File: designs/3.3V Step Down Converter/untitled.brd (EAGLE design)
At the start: 25 x 30 mm, 10 parts, among them IC1 TPS62160DGKR, J1 S2B-PH-SM4, J2 S2B-PH-SM4

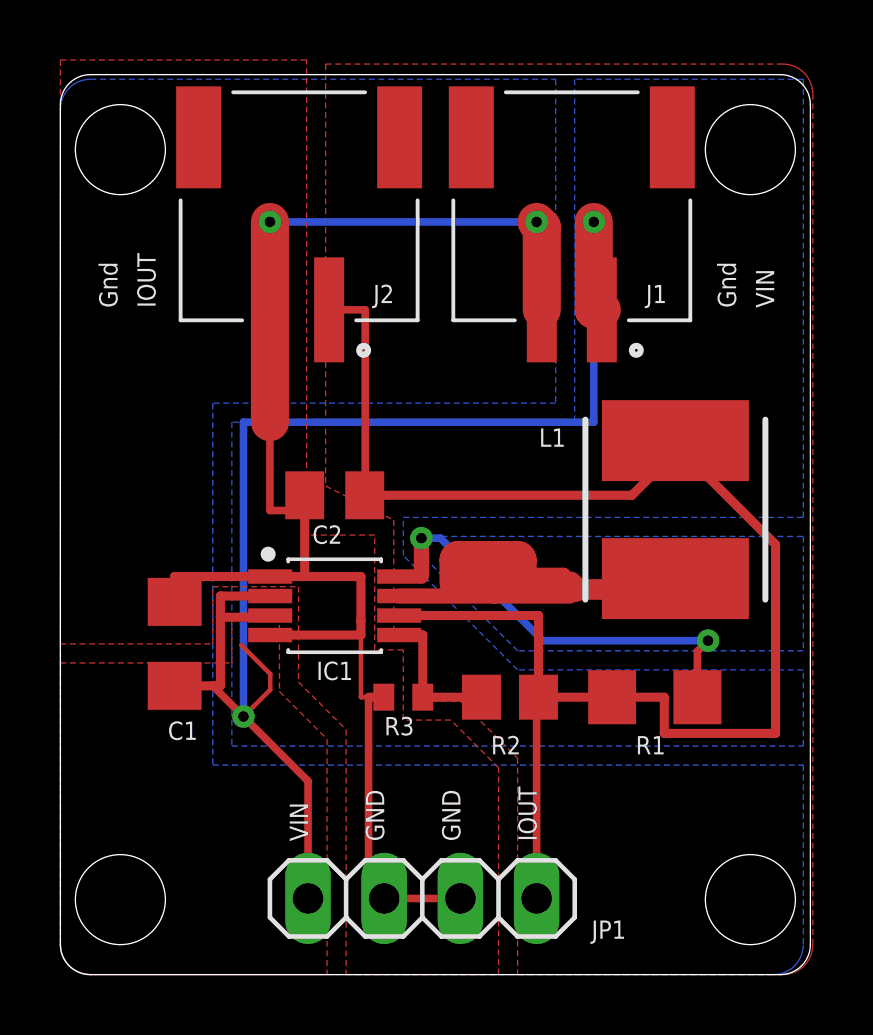
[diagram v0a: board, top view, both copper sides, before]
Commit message: added design block Logo
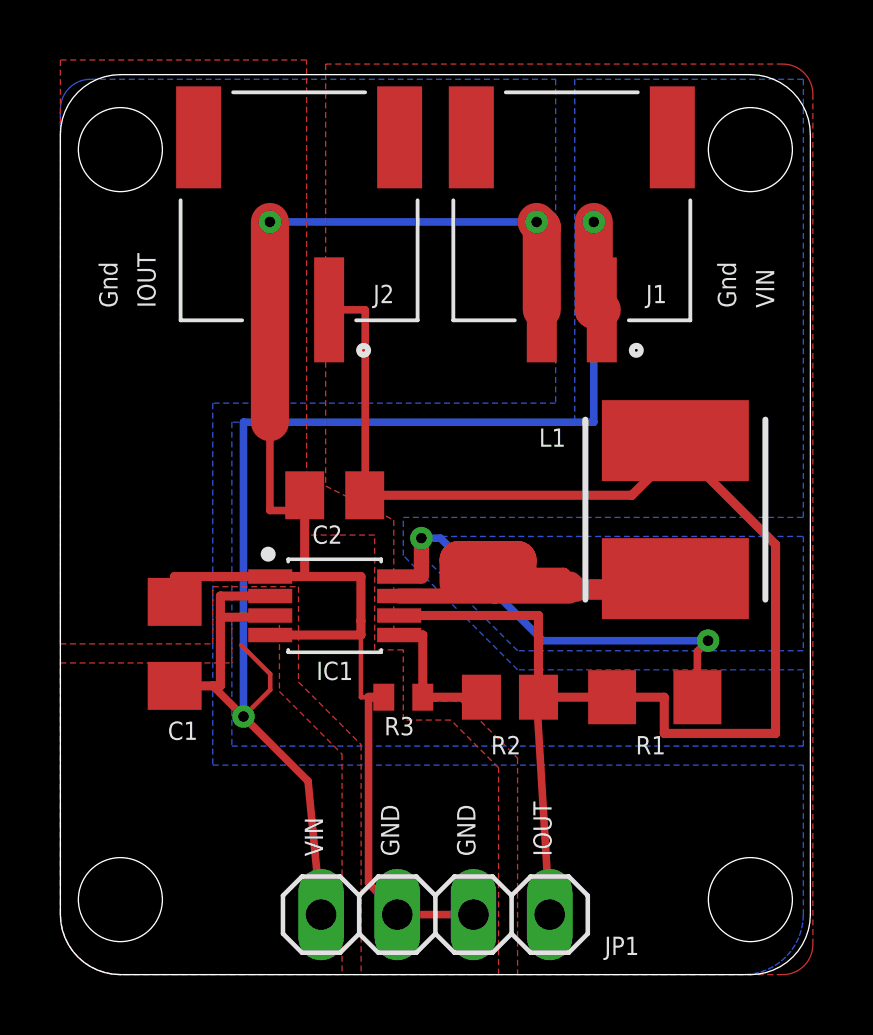
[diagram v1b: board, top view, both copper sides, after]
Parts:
- moved JP1 0.69 mm to (12.5, 2.00)
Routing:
- net AGND: track 55.0 -> 55.7 mm
- net VIN: track 51.9 -> 52.4 mm
- net IOUT: track 53.9 -> 54.4 mm
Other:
- outline, holes or cut-outs redrawn
